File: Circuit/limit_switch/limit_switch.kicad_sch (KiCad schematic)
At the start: 2 parts, among them SW1 XLR3_Ground_Switched

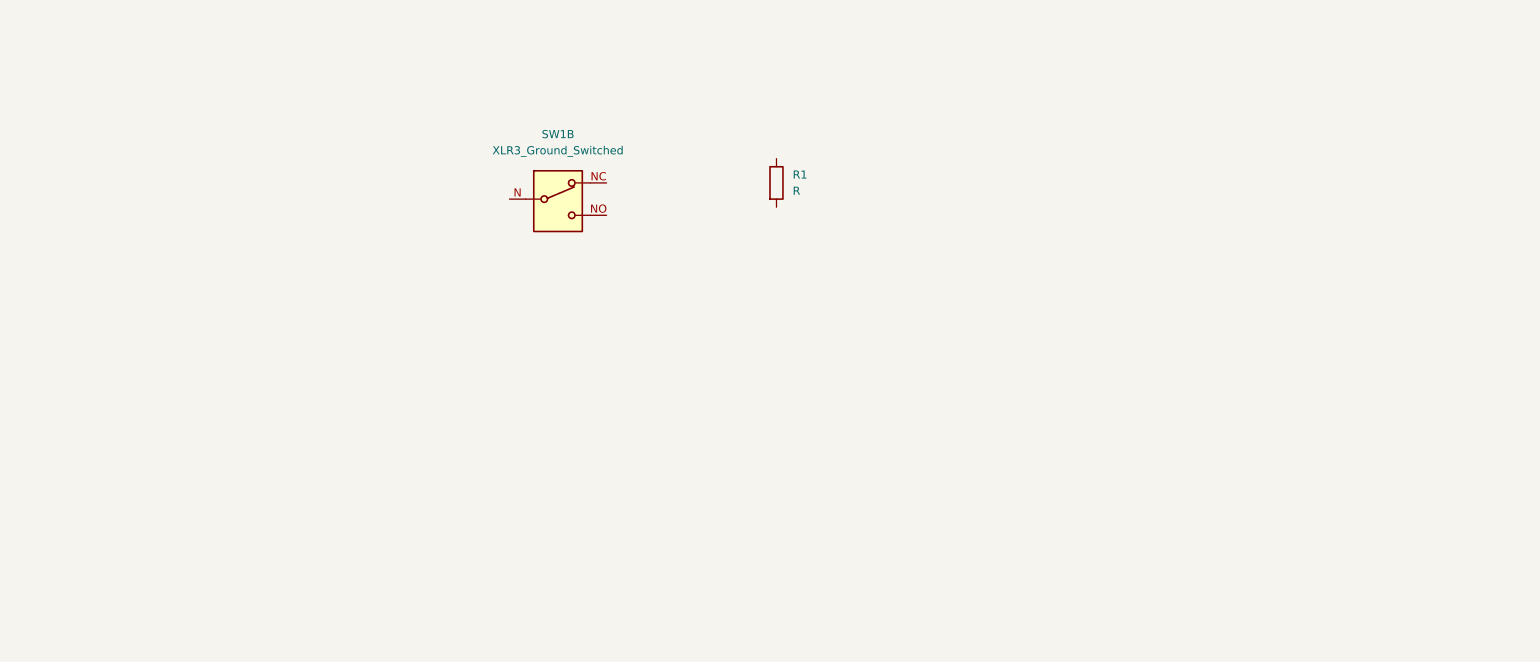
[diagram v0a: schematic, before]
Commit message: Developing limit switch circuit
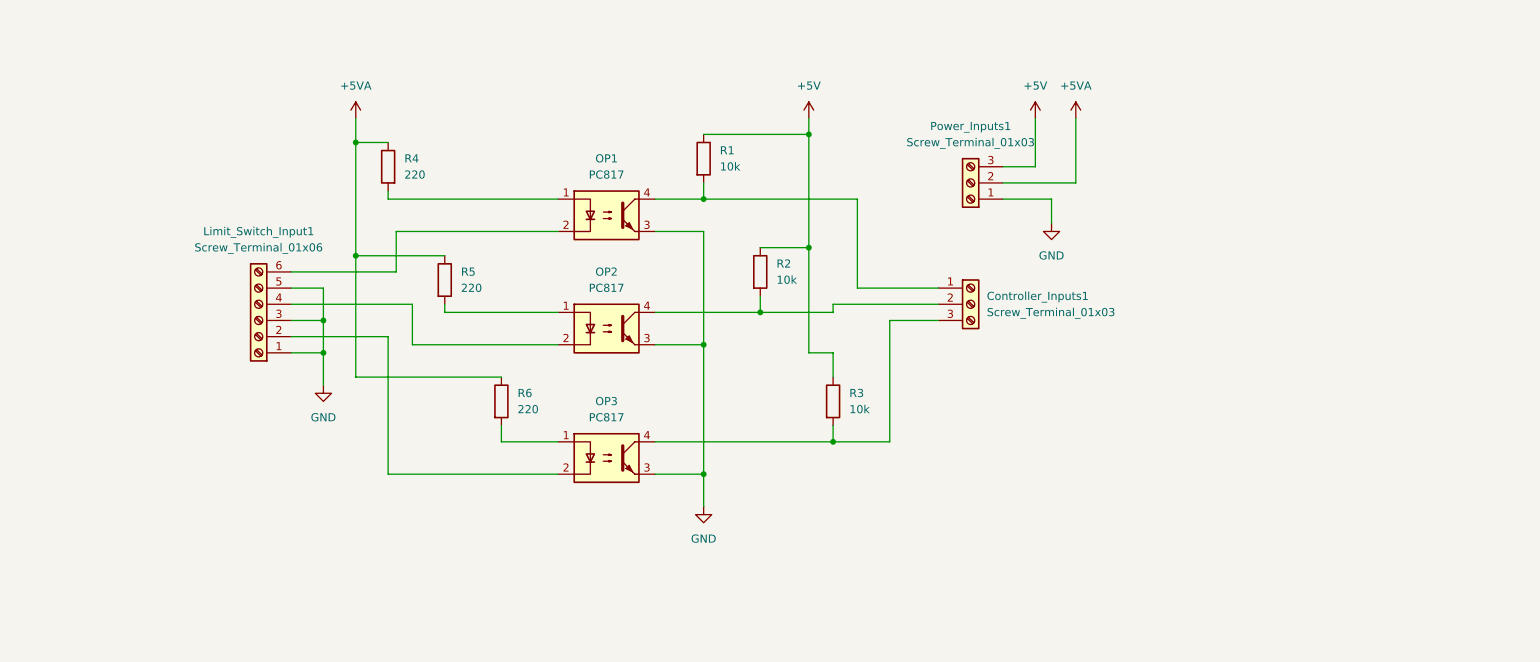
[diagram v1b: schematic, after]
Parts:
- removed SW1: XLR3_Ground_Switched, symbol Connector:XLR3_Ground_Switched
- added Controller_Inputs1, Power_Inputs1: Screw_Terminal_01x03, TerminalBlock:TerminalBlock_bornier-3_P5.08mm, symbol Connector:Screw_Terminal_01x03
- added Limit_Switch_Input1: Screw_Terminal_01x06, TerminalBlock:TerminalBlock_bornier-6_P5.08mm, symbol Connector:Screw_Terminal_01x06
- added OP1, OP2, OP3: PC817, Package_DIP:DIP-4_W7.62mm, symbol Isolator:PC817
- added R2, R3: 10k, Resistor_THT:R_Axial_DIN0207_L6.3mm_D2.5mm_P7.62mm_Horizontal, symbol Device:R
- added R4, R5, R6: 220, Resistor_THT:R_Axial_DIN0207_L6.3mm_D2.5mm_P7.62mm_Horizontal, symbol Device:R
- R1: value R -> 10k; footprint (none) -> Resistor_THT:R_Axial_DIN0207_L6.3mm_D2.5mm_P7.62mm_Horizontal
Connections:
- net +5V: now reaches R1.1
- net +5V: now also Power_Inputs1.3 (Pin_3), R2.1, R3.1
- net at R1.2: now also Controller_Inputs1.1 (Pin_1), OP1.4
- new net: Limit_Switch_Input1.2 (Pin_2), OP3.2
- new net: Limit_Switch_Input1.4 (Pin_4), OP2.2
- new net: Limit_Switch_Input1.6 (Pin_6), OP1.2
- new net: OP1.1, R4.2
- new net: OP3.1, R6.2
- new net: Controller_Inputs1.3 (Pin_3), OP3.4, R3.2
- new net: OP2.1, R5.2
- new net: Controller_Inputs1.2 (Pin_2), OP2.4, R2.2
- new net +5VA: Power_Inputs1.2 (Pin_2), R4.1, R5.1, R6.1
- new net GND: Limit_Switch_Input1.1 (Pin_1), Limit_Switch_Input1.3 (Pin_3), Limit_Switch_Input1.5 (Pin_5), OP1.3, OP2.3, OP3.3, Power_Inputs1.1 (Pin_1)
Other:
- moved on the sheet: R1

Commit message: Finished limit switch circuit and minor changes to cam module
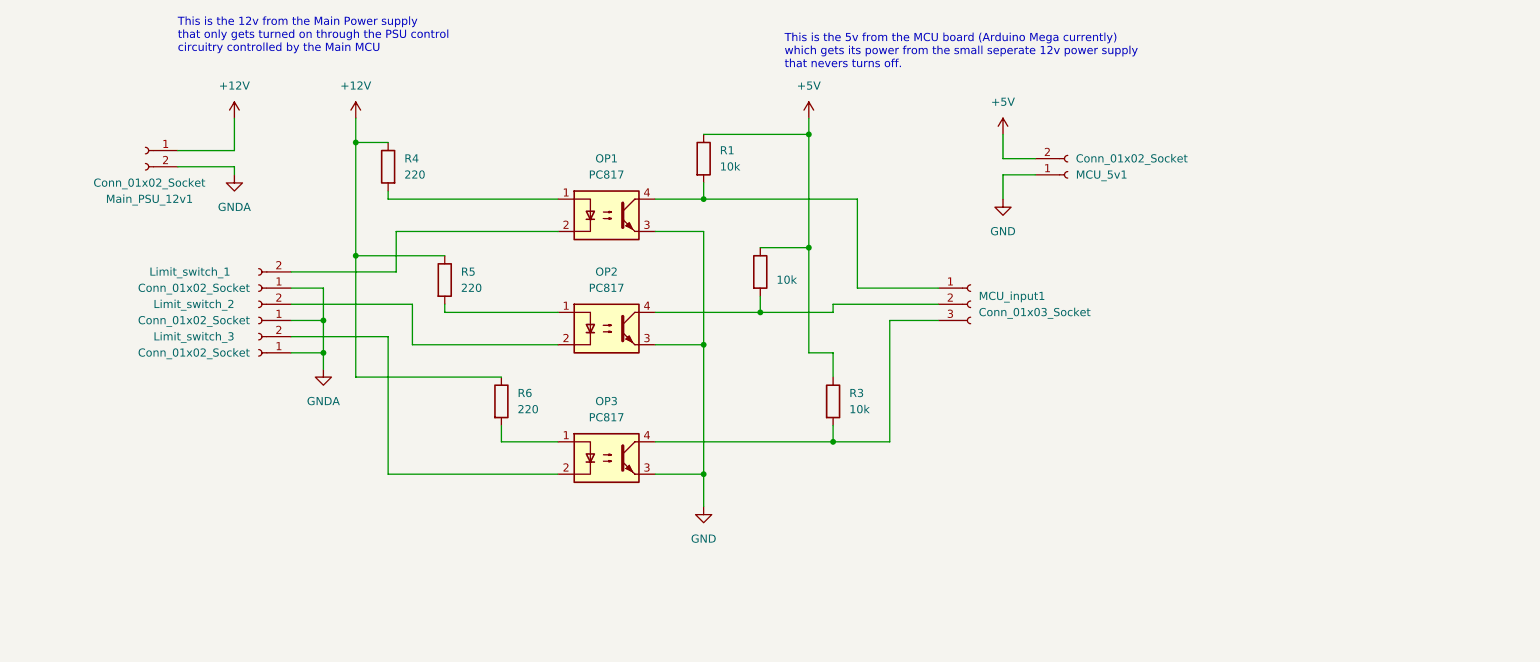
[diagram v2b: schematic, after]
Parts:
- removed Controller_Inputs1, Power_Inputs1: Screw_Terminal_01x03, TerminalBlock:TerminalBlock_bornier-3_P5.08mm, symbol Connector:Screw_Terminal_01x03
- removed Limit_Switch_Input1: Screw_Terminal_01x06, TerminalBlock:TerminalBlock_bornier-6_P5.08mm, symbol Connector:Screw_Terminal_01x06
- added Limit_switch_1, Limit_switch_2, Limit_switch_3, MCU_5v1, Main_PSU_12v1: Conn_01x02_Socket, Connector_PinSocket_2.54mm:PinSocket_1x02_P2.54mm_Horizontal, symbol Connector:Conn_01x02_Socket
- added MCU_input1: Conn_01x03_Socket, Connector_PinSocket_2.54mm:PinSocket_1x03_P2.54mm_Horizontal, symbol Connector:Conn_01x03_Socket
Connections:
- net +5V: now also MCU_5v1.2 (Pin_2)
- net GND: now also MCU_5v1.1 (Pin_1)
- net at OP3.2: now also Limit_switch_3.2 (Pin_2)
- net at OP2.2: now also Limit_switch_2.2 (Pin_2)
- net at OP1.2: now also Limit_switch_1.2 (Pin_2)
- net at OP1.4, R1.2: now also MCU_input1.1 (Pin_1)
- net at OP3.4, R3.2: now also MCU_input1.3 (Pin_3)
- net at OP2.4, R2.2: now also MCU_input1.2 (Pin_2)
- net +5VA renamed +12V
- net +12V: now also Main_PSU_12v1.1 (Pin_1)
- new net GNDA: Limit_switch_1.1 (Pin_1), Limit_switch_2.1 (Pin_1), Limit_switch_3.1 (Pin_1), Main_PSU_12v1.2 (Pin_2)
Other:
- note added: "This is the 12v from the Main Power supply that only gets turned on through the PSU control circuitry controlled by the Main MCU"
- note added: "This is the 5v from the MCU board (Arduino Mega currently) which gets its power from the small seperate 12v power supply that nevers turns off."

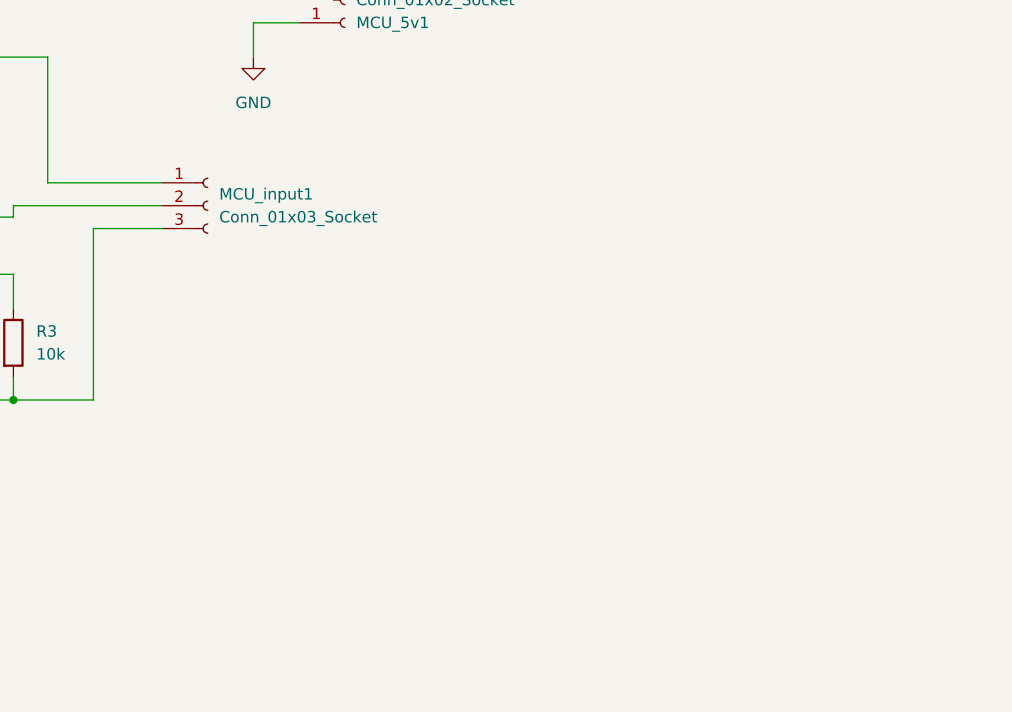
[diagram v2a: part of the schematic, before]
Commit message: added passive filters to limit switch circuit
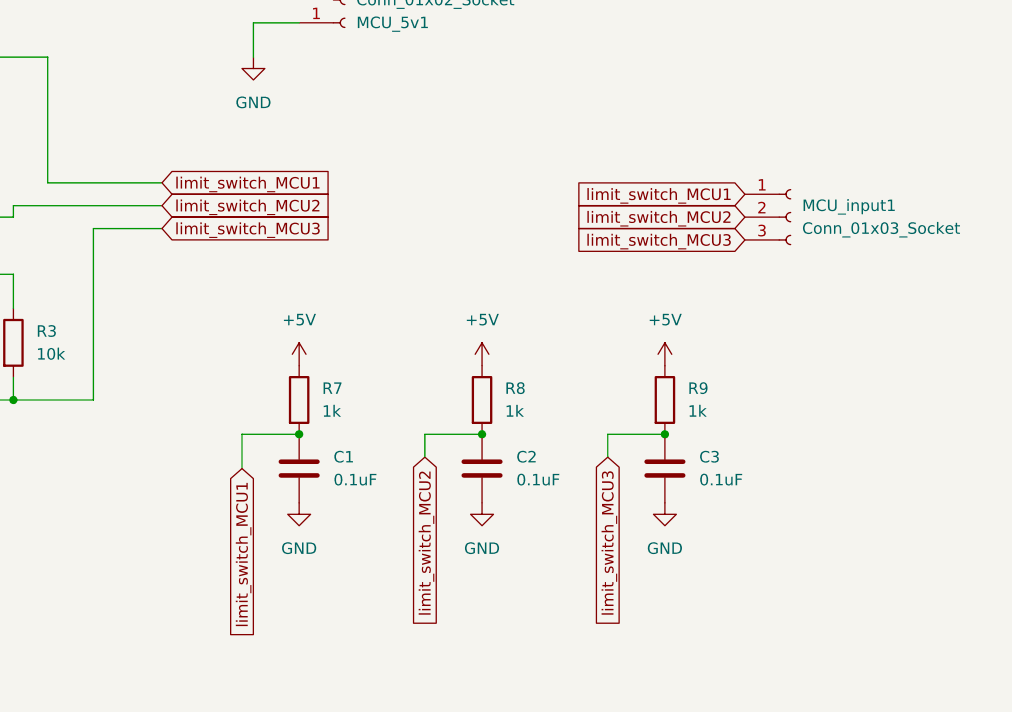
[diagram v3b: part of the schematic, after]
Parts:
- added C1, C2, C3: 0.1uF, Capacitor_THT:C_Disc_D5.0mm_W2.5mm_P5.00mm, symbol Device:C
- added R7, R8, R9: 1k, Resistor_THT:R_Axial_DIN0207_L6.3mm_D2.5mm_P7.62mm_Horizontal, symbol Device:R
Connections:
- net +5V: now also R7.1, R8.1, R9.1
- net GND: now also C1.2, C2.2, C3.2
- net limit_switch_MCU1: now reaches MCU_input1.1 (Pin_1), OP1.4, R1.2
- net limit_switch_MCU1: now also C1.1, R7.2
- net limit_switch_MCU3: now reaches MCU_input1.3 (Pin_3), OP3.4, R3.2
- net limit_switch_MCU3: now also C3.1, R9.2
- net limit_switch_MCU2: now reaches MCU_input1.2 (Pin_2), OP2.4, R2.2
- net limit_switch_MCU2: now also C2.1, R8.2
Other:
- moved on the sheet: MCU_input1

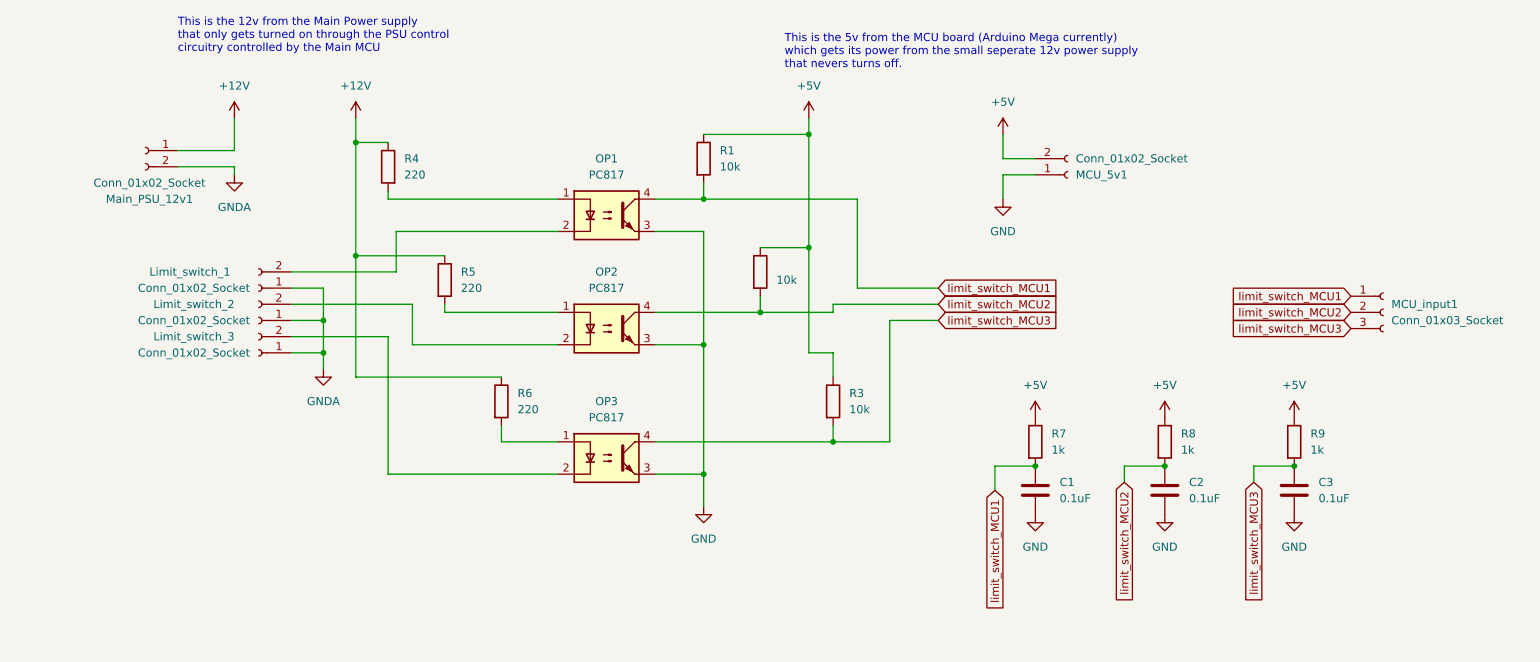
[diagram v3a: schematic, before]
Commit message: Implemented Isolators in PWM Mutliplexer
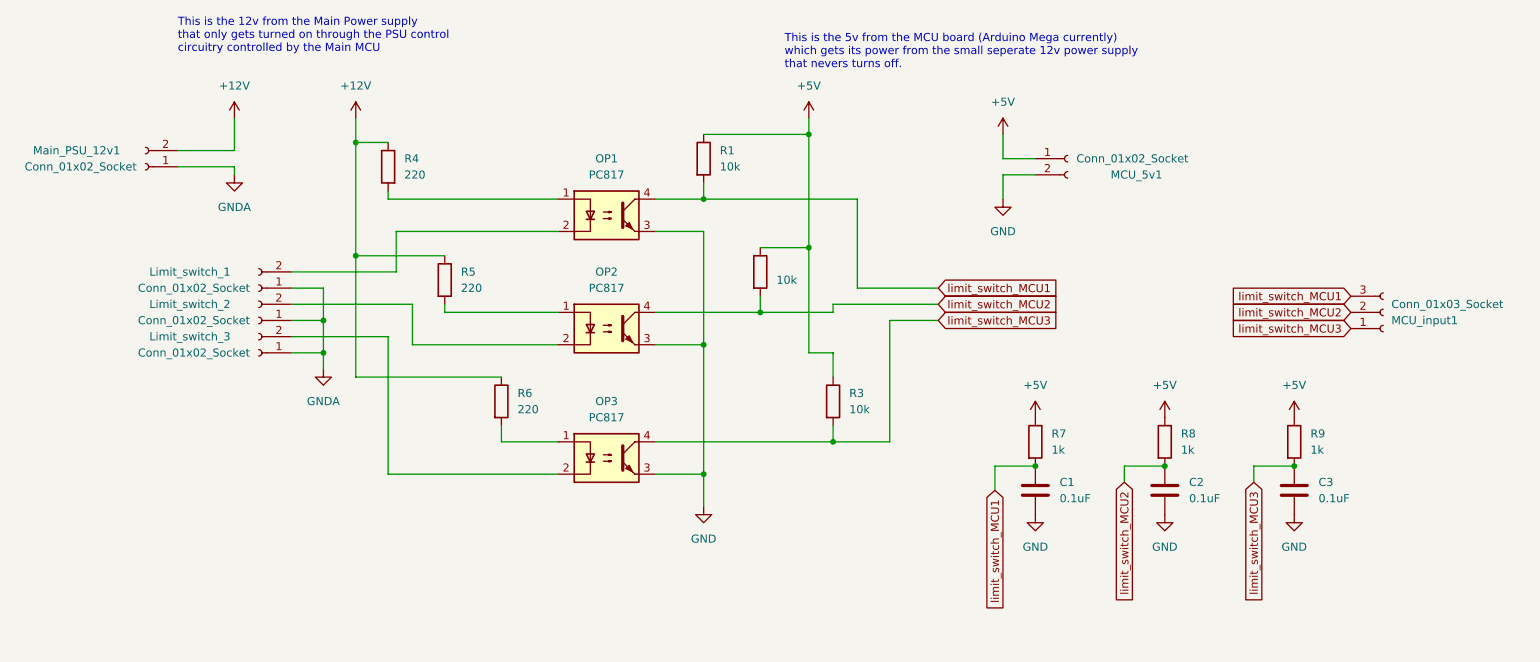
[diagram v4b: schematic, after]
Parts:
- Limit_switch_1, Limit_switch_2, Limit_switch_3, MCU_5v1, Main_PSU_12v1: footprint Connector_PinSocket_2.54mm:PinSocket_1x02_P2.54mm_Horizontal -> Connector_JST:JST_EH_S2B-EH_1x02_P2.50mm_Horizontal
- MCU_input1: footprint Connector_PinSocket_2.54mm:PinSocket_1x03_P2.54mm_Horizontal -> Connector_JST:JST_EH_S3B-EH_1x03_P2.50mm_Horizontal
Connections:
- net +12V: now also Main_PSU_12v1.2 (Pin_2); no longer Main_PSU_12v1.1 (Pin_1)
- net +5V: now also MCU_5v1.1 (Pin_1); no longer MCU_5v1.2 (Pin_2)
- net GND: now also MCU_5v1.2 (Pin_2); no longer MCU_5v1.1 (Pin_1)
- net GNDA: now also Main_PSU_12v1.1 (Pin_1); no longer Main_PSU_12v1.2 (Pin_2)
- net limit_switch_MCU1: now also MCU_input1.3 (Pin_3); no longer MCU_input1.1 (Pin_1)
- net limit_switch_MCU3: now also MCU_input1.1 (Pin_1); no longer MCU_input1.3 (Pin_3)
